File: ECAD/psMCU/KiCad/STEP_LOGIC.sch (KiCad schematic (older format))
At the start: 48 parts, among them U17 SN74LVC1G00DCK, U222 SN74LVC1G175DCK, U223 SN74LVC1G175DCK, U224 SN74LVC1G175DCK, U225 SN74LVC1G32DCK, U226 SN74LVC1G04DCK, U227 SN74LVC1G04DCK, U228 SN74LVC1G04DCK, U229 SN74LVC1G08DCK, U230 SN74LVC1G08DCK, U231 SN74LVC1G04DCK, U232 SN74LVC1G08DCK, U233 SN74LVC1G08DCK, U234 SN74LVC1G08DCK, U235 SN74LVC1G08DCK, U238 SN74LVC1G32DCK, U240 SN74LVC1G08DCK

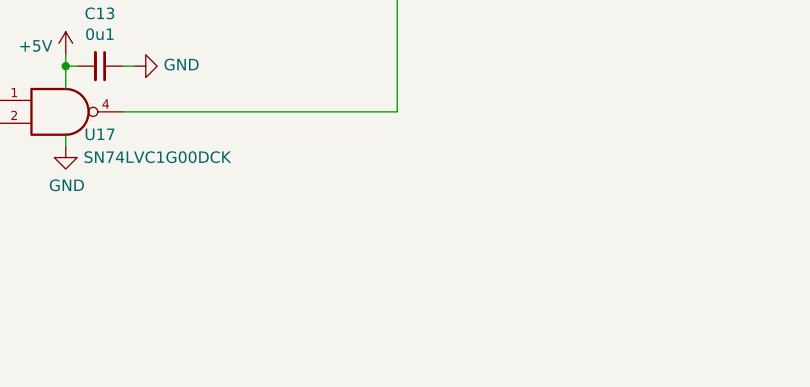
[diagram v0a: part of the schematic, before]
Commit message: Sch: Removed Regulator, Added extra spread bulk C
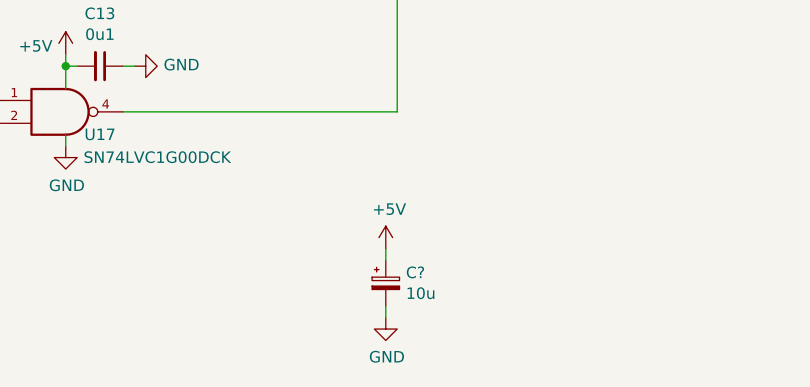
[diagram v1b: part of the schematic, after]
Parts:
- added C?: 10u, symbol Device:CP_Small
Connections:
- net +5V: now also C?.1
- net GND: now also C?.2
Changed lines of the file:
@@
 Wire Wire Line
 	5100 6150 6300 6150
+$Comp
+L Device:CP_Small C?
+U 1 1 626E61DA
+P 6250 6900
+AR Path="/62043340/626E61DA" Ref="C?"  Part="1"
+AR Path="/5FD6B215/626E61DA" Ref="C?"  Part="1"
+F 0 "C?" H 6338 6946 50  0000 L CNN
+F 1 "10u" H 6338 6855 50  0000 L CNN
+F 2 "" H 6250 6900 50  0001 C CNN
+F 3 "~" H 6250 6900 50  0001 C CNN
+	1    6250 6900
+	1    0    0    -1
+$EndComp
+$Comp
+L power:GND #PWR?
+U 1 1 626E61E0
+P 6250 7050
+AR Path="/626E61E0" Ref="#PWR?"  Part="1"
+AR Path="/62043340/626E61E0" Ref="#PWR?"  Part="1"
+AR Path="/5FD6B215/626E61E0" Ref="#PWR?"  Part="1"
+F 0 "#PWR?" H 6250 6800 50  0001 C CNN
+F 1 "GND" H 6255 6877 50  0000 C CNN
+F 2 "" H 6250 7050 50  0001 C CNN
+F 3 "" H 6250 7050 50  0001 C CNN
+	1    6250 7050
+	1    0    0    -1
+$EndComp
+Wire Wire Line
+	6250 7050 6250 7000
+Wire Wire Line
+	6250 6750 6250 6800
+$Comp
+L power:+5V #PWR?
+U 1 1 626E61E8
+P 6250 6750
+AR Path="/626E61E8" Ref="#PWR?"  Part="1"
+AR Path="/62043340/626E61E8" Ref="#PWR?"  Part="1"
+AR Path="/5FD6B215/626E61E8" Ref="#PWR?"  Part="1"
+F 0 "#PWR?" H 6250 6600 50  0001 C CNN
+F 1 "+5V" H 6265 6923 50  0000 C CNN
+F 2 "" H 6250 6750 50  0001 C CNN
+F 3 "" H 6250 6750 50  0001 C CNN
+	1    6250 6750
+	1    0    0    -1
+$EndComp
 $EndSCHEMATC

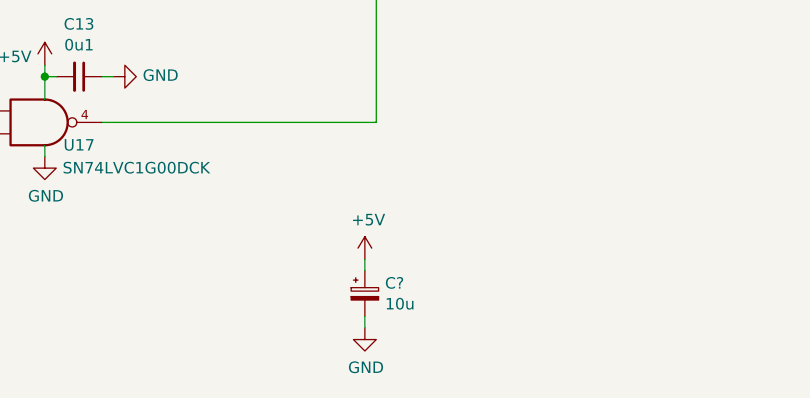
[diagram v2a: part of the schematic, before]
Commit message: Sch: Reworked Peripheral Interface (Buffers)
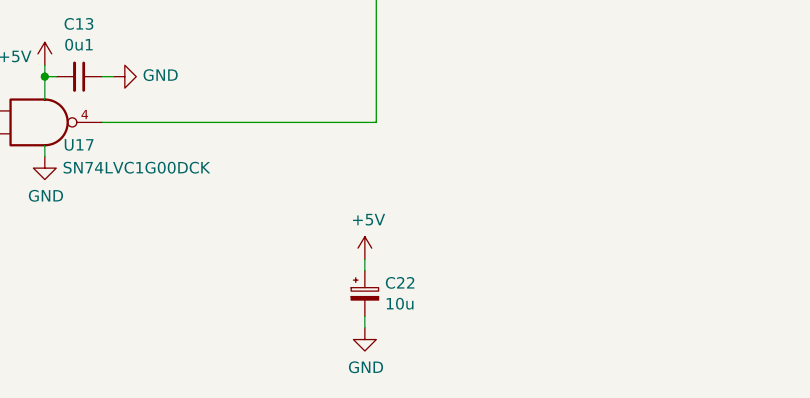
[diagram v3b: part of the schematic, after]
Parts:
- gave numbers to parts that had none: 1
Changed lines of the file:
@@
 $Descr A4 11693 8268
 encoding utf-8
-Sheet 24 97
+Sheet 24 96
 Title "psMCU"
 Date "2022-02-13"
@@
 AR Path="/62043340/626E61DA" Ref="C?"  Part="1"
 AR Path="/5FD6B215/626E61DA" Ref="C?"  Part="1"
-AR Path="/60E33DBC/5F3D6AF9/626E61DA" Ref="C?"  Part="1"
-F 0 "C?" H 6338 6946 50  0000 L CNN
+AR Path="/60E33DBC/5F3D6AF9/626E61DA" Ref="C22"  Part="1"
+F 0 "C22" H 6338 6946 50  0000 L CNN
 F 1 "10u" H 6338 6855 50  0000 L CNN
 F 2 "" H 6250 6900 50  0001 C CNN
@@
 AR Path="/62043340/626E61E0" Ref="#PWR?"  Part="1"
 AR Path="/5FD6B215/626E61E0" Ref="#PWR?"  Part="1"
-AR Path="/60E33DBC/5F3D6AF9/626E61E0" Ref="#PWR?"  Part="1"
-F 0 "#PWR?" H 6250 6800 50  0001 C CNN
+AR Path="/60E33DBC/5F3D6AF9/626E61E0" Ref="#PWR0119"  Part="1"
+F 0 "#PWR0119" H 6250 6800 50  0001 C CNN
 F 1 "GND" H 6255 6877 50  0000 C CNN
 F 2 "" H 6250 7050 50  0001 C CNN
@@
 AR Path="/62043340/626E61E8" Ref="#PWR?"  Part="1"
 AR Path="/5FD6B215/626E61E8" Ref="#PWR?"  Part="1"
-AR Path="/60E33DBC/5F3D6AF9/626E61E8" Ref="#PWR?"  Part="1"
-F 0 "#PWR?" H 6250 6600 50  0001 C CNN
+AR Path="/60E33DBC/5F3D6AF9/626E61E8" Ref="#PWR0120"  Part="1"
+F 0 "#PWR0120" H 6250 6600 50  0001 C CNN
 F 1 "+5V" H 6265 6923 50  0000 C CNN
 F 2 "" H 6250 6750 50  0001 C CNN

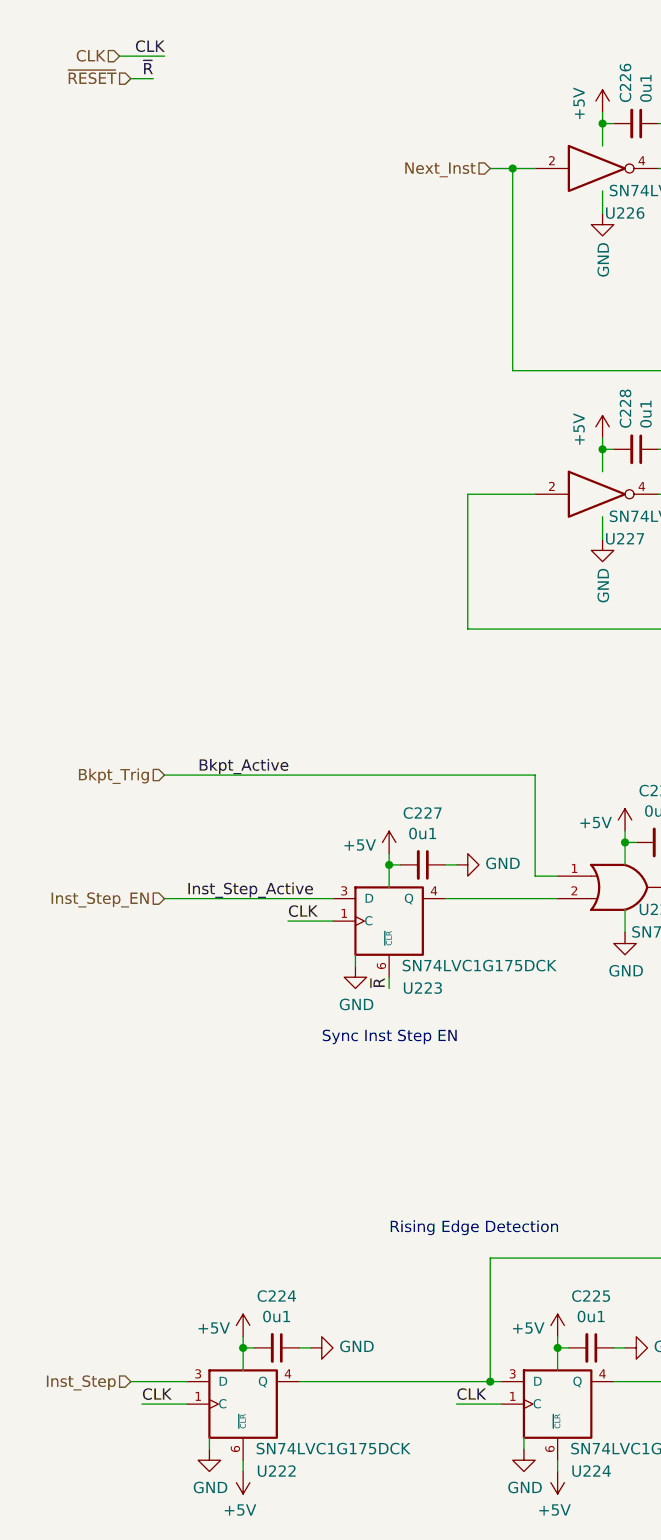
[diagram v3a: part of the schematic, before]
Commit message: Sch: Improved Clk/Reset distribution, moved to global labels
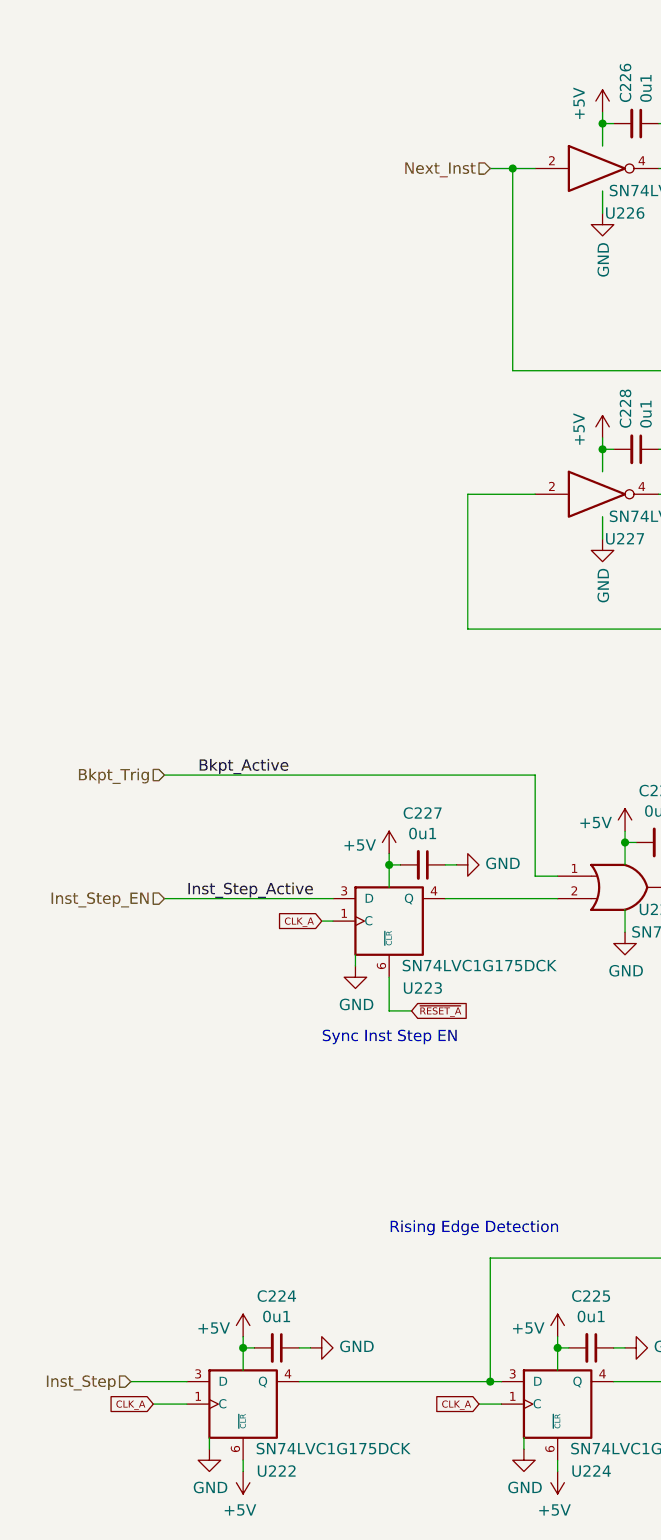
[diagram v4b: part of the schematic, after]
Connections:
- net CLK renamed CLK_A
- net ~RESET renamed ~RESET_A
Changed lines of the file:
@@
 $Descr A4 11693 8268
 encoding utf-8
-Sheet 24 96
+Sheet 24 97
 Title "psMCU"
 Date "2022-02-13"
@@
 Text HLabel 4900 2300 2    50   Output ~ 0
 DO_CLR
-Text HLabel 900  750  0    50   Input ~ 0
-CLK
-Text HLabel 950  850  0    50   Input ~ 0
-~RESET
 $Comp
 L 74xGxx:74LVC1G175 U?
@@
 Wire Wire Line
 	2400 4350 2350 4350
-Text Label 2100 4900 1    50   ~ 0
-~R
-Wire Wire Line
-	2100 4900 2100 4850
-Wire Wire Line
-	950  850  1050 850
-Text Label 1050 850  2    50   ~ 0
-~R
-Wire Wire Line
-	900  750  1100 750
-Text Label 1100 750  2    50   ~ 0
-CLK
-Text Label 1650 4600 0    50   ~ 0
-CLK
-Wire Wire Line
-	1650 4600 1850 4600
 $Comp
 L 74xGxx:74LVC1G32 U?
@@
 	2600 6650 2550 6650
 Wire Wire Line
-	2850 7050 2850 7000
-$Comp
-L power:+5V #PWR?
-U 1 1 611775E5
-P 2850 7050
-AR Path="/5ED2705B/611775E5" Ref="#PWR?"  Part="1"
-AR Path="/5F1CE57C/611775E5" Ref="#PWR?"  Part="1"
-AR Path="/5F396002/611775E5" Ref="#PWR?"  Part="1"
-AR Path="/608BF85D/60010AFF/611775E5" Ref="#PWR?"  Part="1"
-AR Path="/60E33DBC/5F3D6AF9/611775E5" Ref="#PWR0517"  Part="1"
-F 0 "#PWR0517" H 2850 6900 50  0001 C CNN
-F 1 "+5V" H 2865 7223 50  0000 C CNN
-F 2 "" H 2850 7050 50  0001 C CNN
-F 3 "" H 2850 7050 50  0001 C CNN
-	1    2850 7050
-	-1   0    0    1
-$EndComp
-Wire Wire Line
 	1450 7050 1450 7000
 $Comp
@@
 Wire Wire Line
 	2550 6100 4550 6100
-Text Label 1000 6750 0    50   ~ 0
-CLK
-Wire Wire Line
-	1000 6750 1200 6750
-Text Label 2400 6750 0    50   ~ 0
-CLK
-Wire Wire Line
-	2400 6750 2600 6750
 Text Notes 2100 6000 0    50   ~ 0
 Rising Edge Detection
@@
 	1    0    0    -1
 $EndComp
+Wire Wire Line
+	2850 7050 2850 7000
+Text GLabel 1800 4600 0    31   Input ~ 0
+CLK_A
+Wire Wire Line
+	1800 4600 1850 4600
+Text GLabel 2200 5000 2    31   Input ~ 0
+~RESET_A
+Wire Wire Line
+	2200 5000 2100 5000
+Wire Wire Line
+	2100 5000 2100 4850
+Text GLabel 2500 6750 0    31   Input ~ 0
+CLK_A
+$Comp
+L power:+5V #PWR?
+U 1 1 611775E5
+P 2850 7050
+AR Path="/5ED2705B/611775E5" Ref="#PWR?"  Part="1"
+AR Path="/5F1CE57C/611775E5" Ref="#PWR?"  Part="1"
+AR Path="/5F396002/611775E5" Ref="#PWR?"  Part="1"
+AR Path="/608BF85D/60010AFF/611775E5" Ref="#PWR?"  Part="1"
+AR Path="/60E33DBC/5F3D6AF9/611775E5" Ref="#PWR0517"  Part="1"
+F 0 "#PWR0517" H 2850 6900 50  0001 C CNN
+F 1 "+5V" H 2865 7223 50  0000 C CNN
+F 2 "" H 2850 7050 50  0001 C CNN
+F 3 "" H 2850 7050 50  0001 C CNN
+	1    2850 7050
+	-1   0    0    1
+$EndComp
+Wire Wire Line
+	2500 6750 2600 6750
+Text GLabel 1050 6750 0    31   Input ~ 0
+CLK_A
+Wire Wire Line
+	1050 6750 1200 6750
 $EndSCHEMATC
